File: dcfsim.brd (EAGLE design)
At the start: 33.5 x 53.3 mm, 17 parts, among them U1 ATTINY45-20P

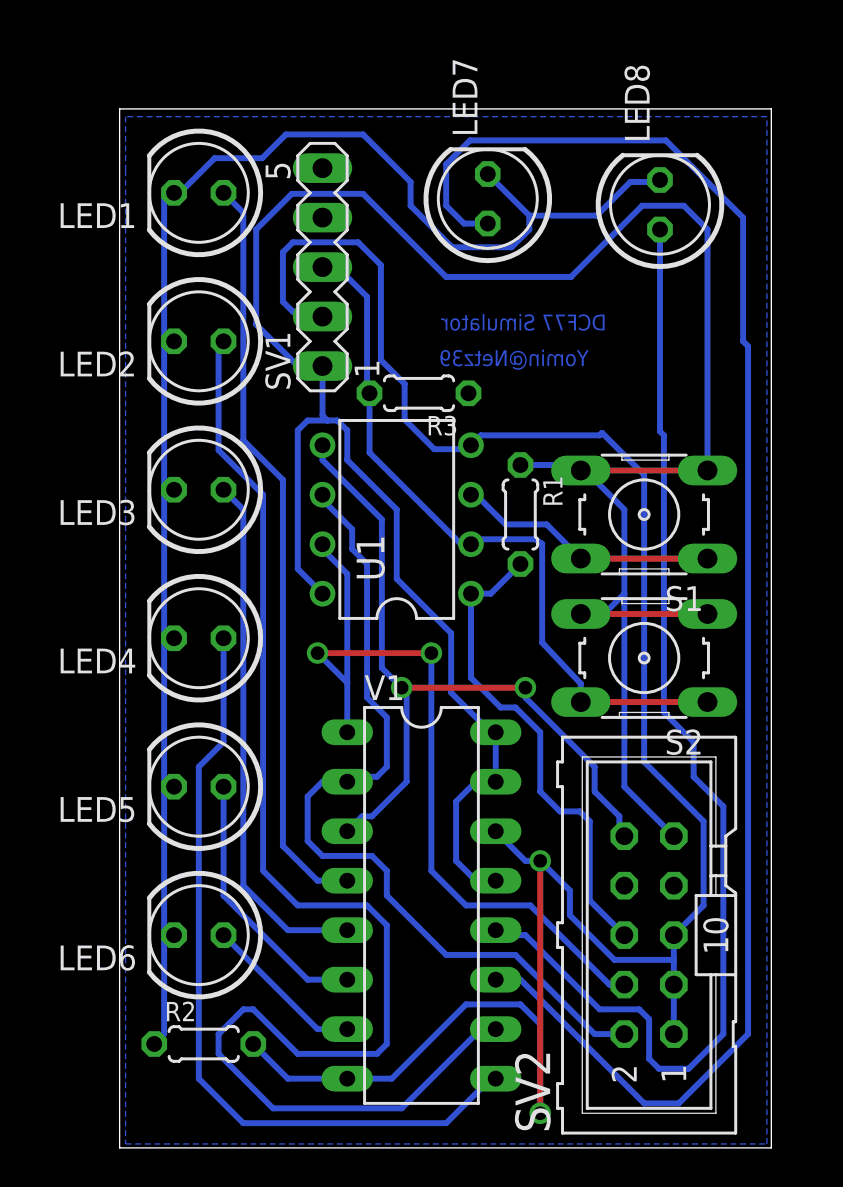
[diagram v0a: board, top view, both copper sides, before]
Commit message: rename clockset to dcfsim, move buttons upwards, move text to doc layer
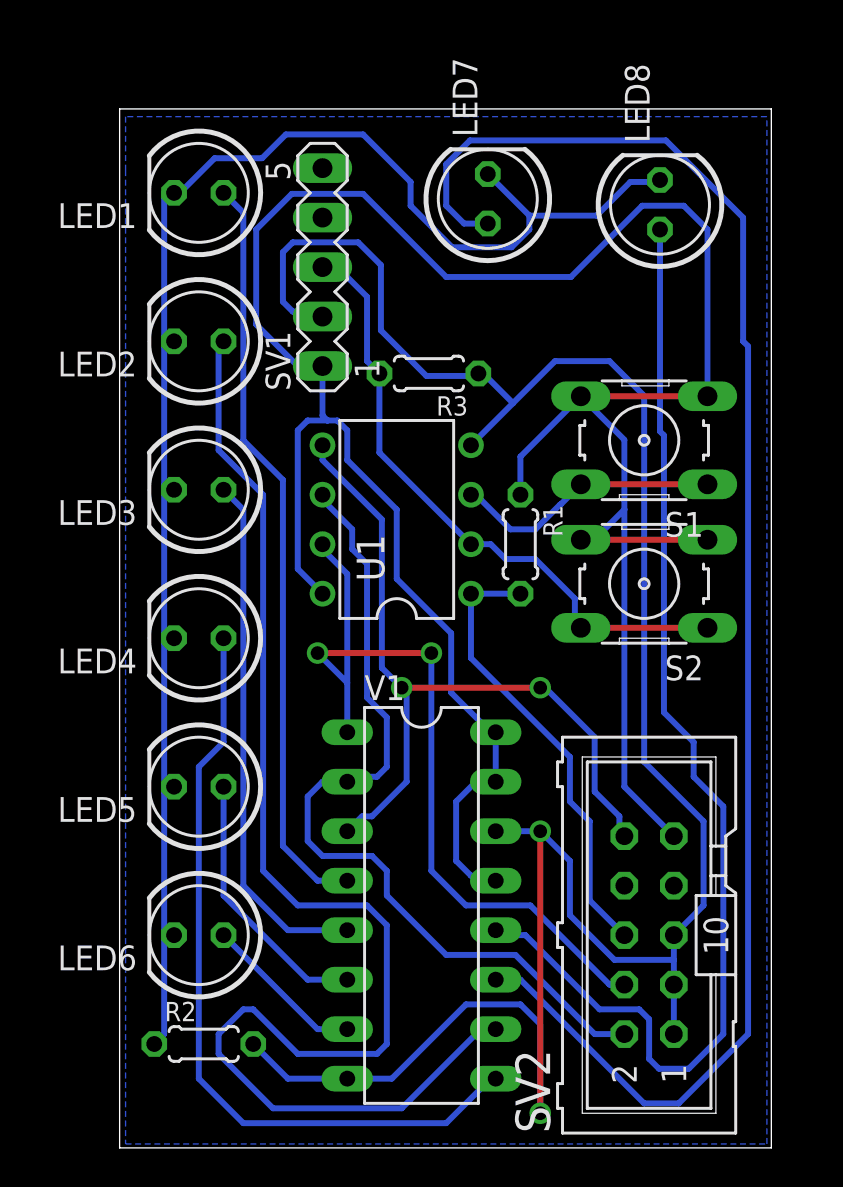
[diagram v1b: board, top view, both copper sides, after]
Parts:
- moved S1 3.81 mm to (26.9, 63.2)
- moved S2 3.81 mm to (26.9, 55.9)
- moved R1 1.52 mm to (20.6, 57.9)
- moved R3 1.14 mm to (15.9, 66.7)
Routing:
- net GND: track 111.4 -> 118.6 mm
- net N$5: track 37.4 -> 32.4 mm
- net +5V: track 133.1 -> 136.3 mm
- net N$1: track 25.0 -> 23.3 mm
- net N$4: track 39.2 -> 39.8 mm
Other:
- board text added: "DCF77 Simulator v1"
- board text removed: "DCF77 Simulator"

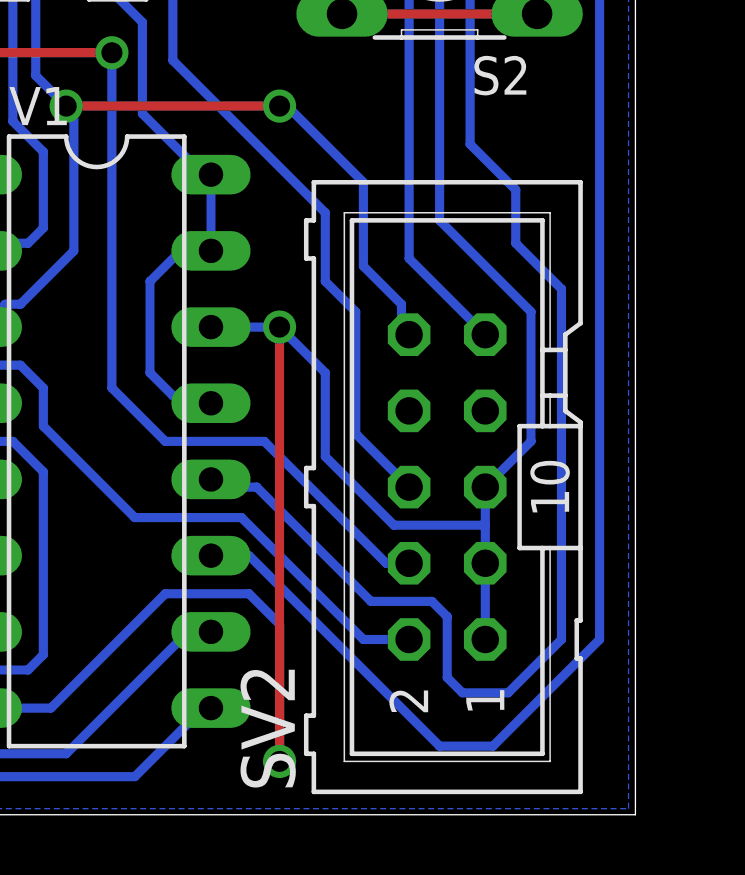
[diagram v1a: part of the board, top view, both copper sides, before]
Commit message: rotate isp 180°, connect 4th gnd pin, move logo/text to doc layer
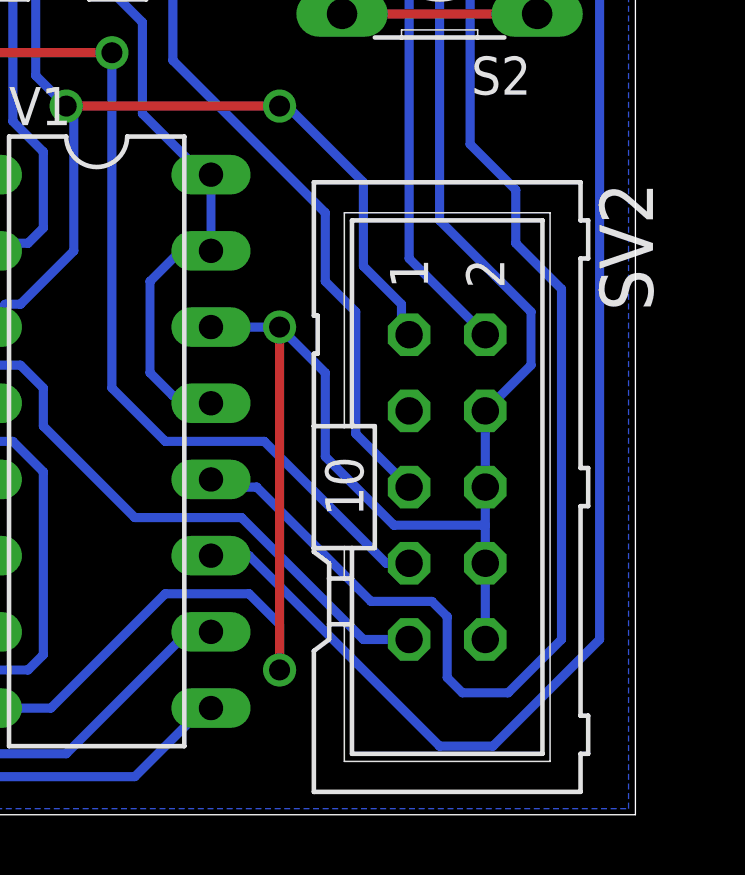
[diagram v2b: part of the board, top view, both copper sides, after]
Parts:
- turned SV2 to 270 degrees
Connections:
- net +5V: now also SV2.2; no longer SV2.9
- net GND: now also SV2.10, SV2.4, SV2.6, SV2.8; no longer SV2.1, SV2.3, SV2.5
- net N$1: now also SV2.5; no longer SV2.6
- net N$2: now also SV2.7; no longer SV2.4
- net N$3: now also SV2.9; no longer SV2.2
- net N$4: now also SV2.1; no longer SV2.10
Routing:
- net GND: track 118.6 -> 112.5 mm
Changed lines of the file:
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@@
 <attribute name="OC_FARNELL" value="unknown" x="10.414" y="72.136" size="1.778" layer="27" rot="R90" display="off"/>
 </element>
-<element name="SV2" library="con-harting-ml" package="ML10" value="ISP" x="27.178" y="37.846" rot="R90">
-<attribute name="OC_NEWARK" value="unknown" x="27.178" y="37.846" size="1.778" layer="27" rot="R90" display="off"/>
-<attribute name="MPN" value="" x="27.178" y="37.846" size="1.778" layer="27" rot="R90" display="off"/>
-<attribute name="MF" value="" x="27.178" y="37.846" size="1.778" layer="27" rot="R90" display="off"/>
-<attribute name="OC_FARNELL" value="unknown" x="27.178" y="37.846" size="1.778" layer="27" rot="R90" display="off"/>
+<element name="SV2" library="con-harting-ml" package="ML10" value="ISP" x="27.178" y="37.846" rot="R270">
+<attribute name="OC_NEWARK" value="unknown" x="27.178" y="37.846" size="1.778" layer="27" rot="R270" display="off"/>
+<attribute name="MPN" value="" x="27.178" y="37.846" size="1.778" layer="27" rot="R270" display="off"/>
+<attribute name="MF" value="" x="27.178" y="37.846" size="1.778" layer="27" rot="R270" display="off"/>
+<attribute name="OC_FARNELL" value="unknown" x="27.178" y="37.846" size="1.778" layer="27" rot="R270" display="off"/>
 </element>
 <element name="LED8" library="led" package="LED5MM" value="TIME TYPE 2" x="27.7368" y="75.3364" rot="R90"/>
@@
 <signal name="GND">
 <contactref element="U1" pad="4"/>
-<contactref element="SV2" pad="5"/>
-<contactref element="SV2" pad="3"/>
-<contactref element="SV2" pad="1"/>
 <contactref element="U1" pad="4"/>
 <contactref element="SV1" pad="2"/>
@@
 <wire x1="26.924" y1="65.532" x2="26.924" y2="46.736" width="0.3048" layer="16"/>
 <wire x1="26.924" y1="46.736" x2="29.972" y2="43.688" width="0.3048" layer="16"/>
-<wire x1="29.972" y1="43.688" x2="29.972" y2="39.37" width="0.3048" layer="16"/>
-<wire x1="29.972" y1="39.37" x2="28.448" y2="37.846" width="0.3048" layer="16"/>
-<wire x1="28.448" y1="37.846" x2="28.448" y2="36.576" width="0.3048" layer="16"/>
-<wire x1="28.448" y1="36.576" x2="28.448" y2="32.766" width="0.3048" layer="16"/>
 <wire x1="25.4" y1="36.576" x2="28.448" y2="36.576" width="0.3048" layer="16"/>
 <wire x1="11.684" y1="30.48" x2="13.97" y2="30.48" width="0.3048" layer="16"/>
@@
 <wire x1="20.574" y1="34.29" x2="21.59" y2="33.274" width="0.3048" layer="16"/>
 <via x="21.59" y="43.18" extent="1-16" drill="0.7" shape="octagon"/>
-<via x="21.59" y="28.702" extent="1-16" drill="0.7" shape="octagon"/>
-<wire x1="21.59" y1="43.18" x2="21.59" y2="28.702" width="0.3048" layer="1"/>
-<wire x1="21.59" y1="33.274" x2="21.59" y2="28.702" width="0.3048" layer="16"/>
+<via x="21.59" y="31.75" extent="1-16" drill="0.7" shape="octagon"/>
+<wire x1="21.59" y1="43.18" x2="21.59" y2="31.75" width="0.3048" layer="1"/>
+<wire x1="21.59" y1="33.274" x2="21.59" y2="31.75" width="0.3048" layer="16"/>
 <wire x1="25.4" y1="36.576" x2="23.114" y2="38.862" width="0.3048" layer="16"/>
 <wire x1="12.2428" y1="73.406" x2="8.89" y2="73.406" width="0.3048" layer="16"/>
@@
 <wire x1="23.114" y1="38.862" x2="23.114" y2="41.656" width="0.3048" layer="16"/>
 <wire x1="23.114" y1="41.656" x2="21.59" y2="43.18" width="0.3048" layer="16"/>
+<contactref element="SV2" pad="10"/>
+<contactref element="SV2" pad="8"/>
+<contactref element="SV2" pad="6"/>
+<contactref element="SV2" pad="4"/>
+<wire x1="29.972" y1="43.688" x2="29.972" y2="41.91" width="0.3048" layer="16"/>
+<wire x1="29.972" y1="41.91" x2="28.448" y2="40.386" width="0.3048" layer="16"/>
+<wire x1="28.448" y1="40.386" x2="28.448" y2="37.846" width="0.3048" layer="16"/>
+<wire x1="28.448" y1="37.846" x2="28.448" y2="35.306" width="0.3048" layer="16"/>
+<wire x1="28.448" y1="35.306" x2="28.448" y2="32.766" width="0.3048" layer="16"/>
 </signal>
 <signal name="N$1">
 <contactref element="U1" pad="1"/>
-<contactref element="SV2" pad="6"/>
 <contactref element="R1" pad="2"/>
 <wire x1="24.13" y1="43.688" x2="24.13" y2="39.624" width="0.3048" layer="16"/>
-<wire x1="24.13" y1="39.624" x2="25.908" y2="37.846" width="0.3048" layer="16"/>
 <wire x1="18.034" y1="55.372" x2="20.574" y2="55.372" width="0.3048" layer="16"/>
 <wire x1="18.034" y1="52.07" x2="23.114" y2="46.99" width="0.3048" layer="16"/>
@@
 <wire x1="23.114" y1="44.704" x2="24.13" y2="43.688" width="0.3048" layer="16"/>
 <wire x1="18.034" y1="55.372" x2="18.034" y2="52.07" width="0.3048" layer="16"/>
+<contactref element="SV2" pad="5"/>
+<wire x1="24.13" y1="39.624" x2="25.908" y2="37.846" width="0.3048" layer="16"/>
 </signal>
 <signal name="N$2">
 <contactref element="U1" pad="7"/>
-<contactref element="SV2" pad="4"/>
 <contactref element="V1" pad="1"/>
-<wire x1="25.908" y1="35.306" x2="25.146" y2="35.306" width="0.3048" layer="16"/>
 <wire x1="25.146" y1="35.306" x2="21.082" y2="39.37" width="0.3048" layer="16"/>
 <wire x1="21.082" y1="39.37" x2="17.78" y2="39.37" width="0.3048" layer="16"/>
@@
 <wire x1="16.002" y1="41.148" x2="16.002" y2="52.324" width="0.3048" layer="16"/>
 <wire x1="10.16" y1="52.324" x2="11.684" y2="50.8" width="0.3048" layer="16"/>
+<contactref element="SV2" pad="7"/>
+<wire x1="25.146" y1="35.306" x2="25.908" y2="35.306" width="0.3048" layer="16"/>
 </signal>
 <signal name="N$3">
 <contactref element="U1" pad="6"/>
-<contactref element="SV2" pad="2"/>
 <contactref element="V1" pad="2"/>
-<wire x1="25.908" y1="32.766" x2="24.384" y2="32.766" width="0.3048" layer="16"/>
 <wire x1="24.384" y1="32.766" x2="20.32" y2="36.83" width="0.3048" layer="16"/>
 <wire x1="20.32" y1="36.83" x2="16.764" y2="36.83" width="0.3048" layer="16"/>
@@
 <wire x1="13.208" y1="45.974" x2="11.938" y2="45.974" width="0.3048" layer="16"/>
 <wire x1="11.938" y1="45.974" x2="11.684" y2="45.72" width="0.3048" layer="16"/>
+<contactref element="SV2" pad="9"/>
+<wire x1="24.384" y1="32.766" x2="25.908" y2="32.766" width="0.3048" layer="16"/>
 </signal>
 <signal name="N$4">
 <contactref element="U1" pad="5"/>
-<contactref element="SV2" pad="10"/>
 <contactref element="V1" pad="3"/>
 <wire x1="14.732" y1="45.72" x2="12.954" y2="43.942" width="0.3048" layer="16"/>
@@
 <wire x1="24.384" y1="45.212" x2="25.654" y2="43.942" width="0.3048" layer="16"/>
 <wire x1="25.654" y1="43.942" x2="25.654" y2="43.18" width="0.3048" layer="16"/>
-<wire x1="25.654" y1="43.18" x2="25.908" y2="42.926" width="0.3048" layer="16"/>
 <wire x1="10.414" y1="62.992" x2="10.414" y2="62.23" width="0.3048" layer="16"/>
 <wire x1="10.414" y1="62.23" x2="13.462" y2="59.182" width="0.3048" layer="16"/>
@@
 <wire x1="21.844" y1="50.546" x2="24.384" y2="48.006" width="0.3048" layer="16"/>
 <wire x1="24.384" y1="48.006" x2="24.384" y2="45.212" width="0.3048" layer="16"/>
+<contactref element="SV2" pad="1"/>
+<wire x1="25.654" y1="43.18" x2="25.908" y2="42.926" width="0" layer="19" extent="16-16"/>
 </signal>
 <signal name="+5V">
-<contactref element="SV2" pad="9"/>
 <contactref element="U1" pad="8"/>
 <contactref element="R1" pad="1"/>
@@
 <wire x1="25.908" y1="63.2714" x2="25.908" y2="59.69" width="0.3048" layer="16"/>
 <wire x1="25.908" y1="59.69" x2="25.908" y2="45.466" width="0.3048" layer="16"/>
-<wire x1="25.908" y1="45.466" x2="28.448" y2="42.926" width="0.3048" layer="16"/>
 <wire x1="19.304" y1="45.72" x2="18.288" y2="45.72" width="0.3048" layer="16"/>
 <wire x1="18.288" y1="45.72" x2="17.272" y2="44.704" width="0.3048" layer="16"/>
@@
 <wire x1="23.6728" y1="58.1406" x2="24.3586" y2="58.1406" width="0.3048" layer="16"/>
 <wire x1="24.3586" y1="58.1406" x2="25.908" y2="59.69" width="0.3048" layer="16"/>
+<contactref element="SV2" pad="2"/>
+<wire x1="25.908" y1="45.466" x2="28.448" y2="42.926" width="0.3048" layer="16"/>
 </signal>
 <signal name="N$13">
